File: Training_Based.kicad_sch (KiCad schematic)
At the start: 66 parts

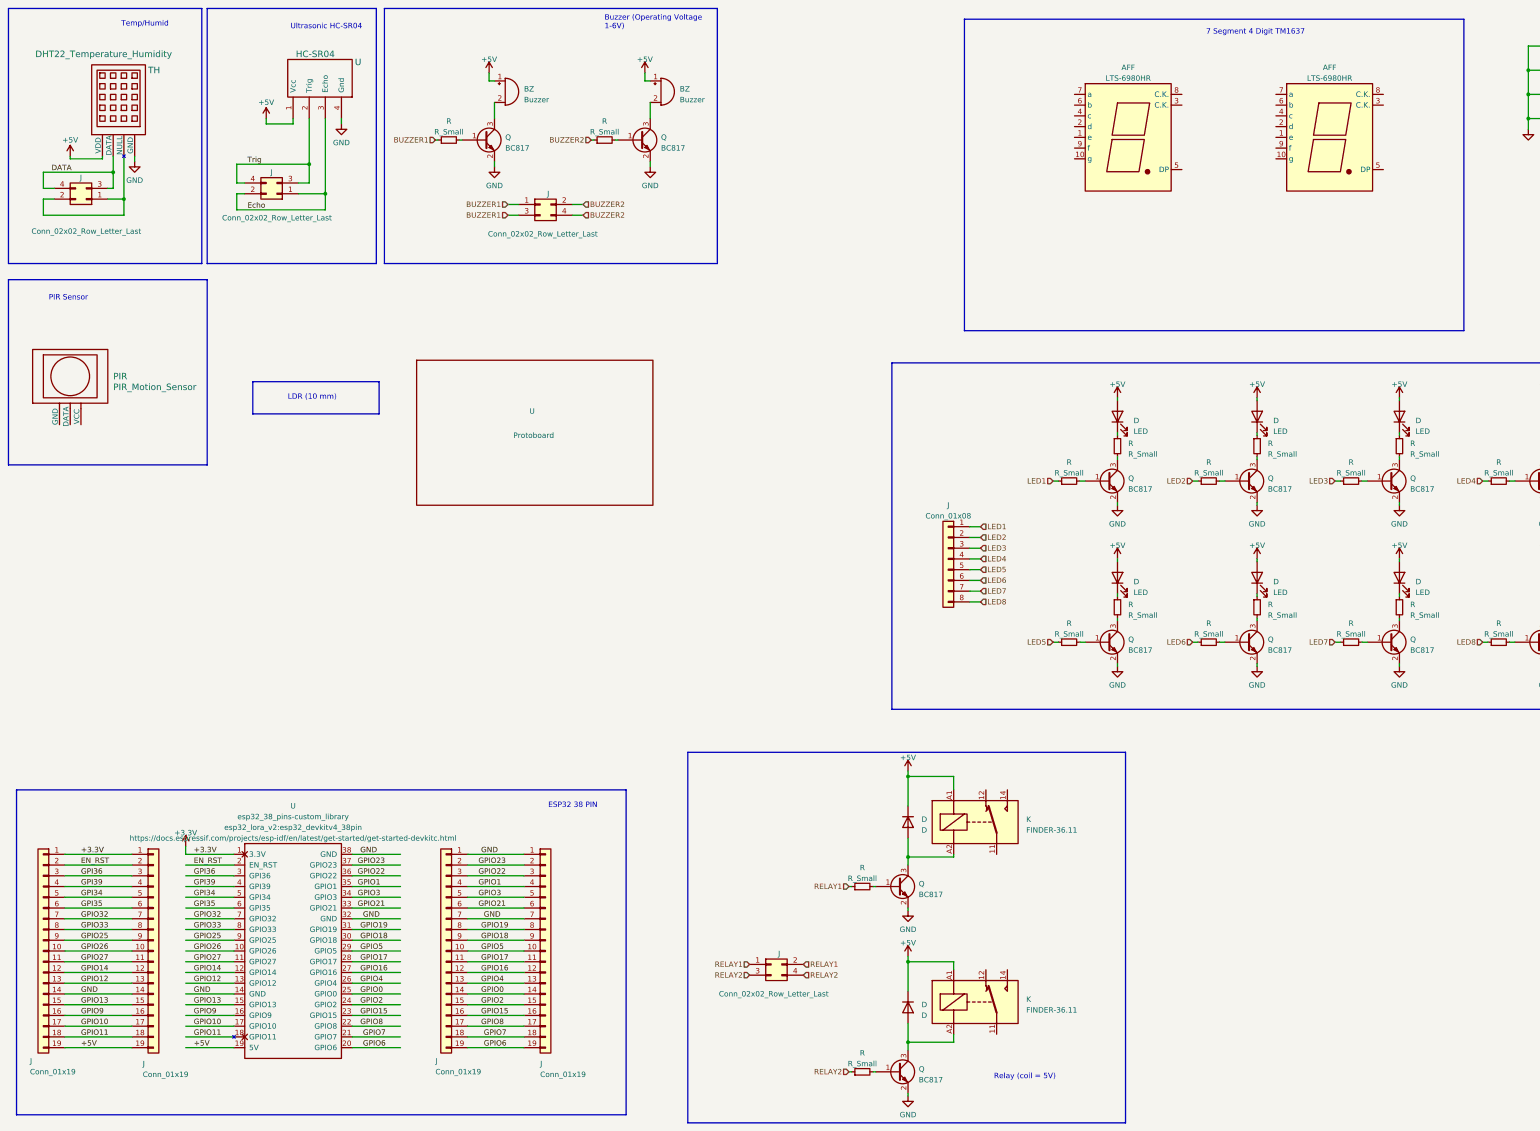
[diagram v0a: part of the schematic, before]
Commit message: 7 segment and relay
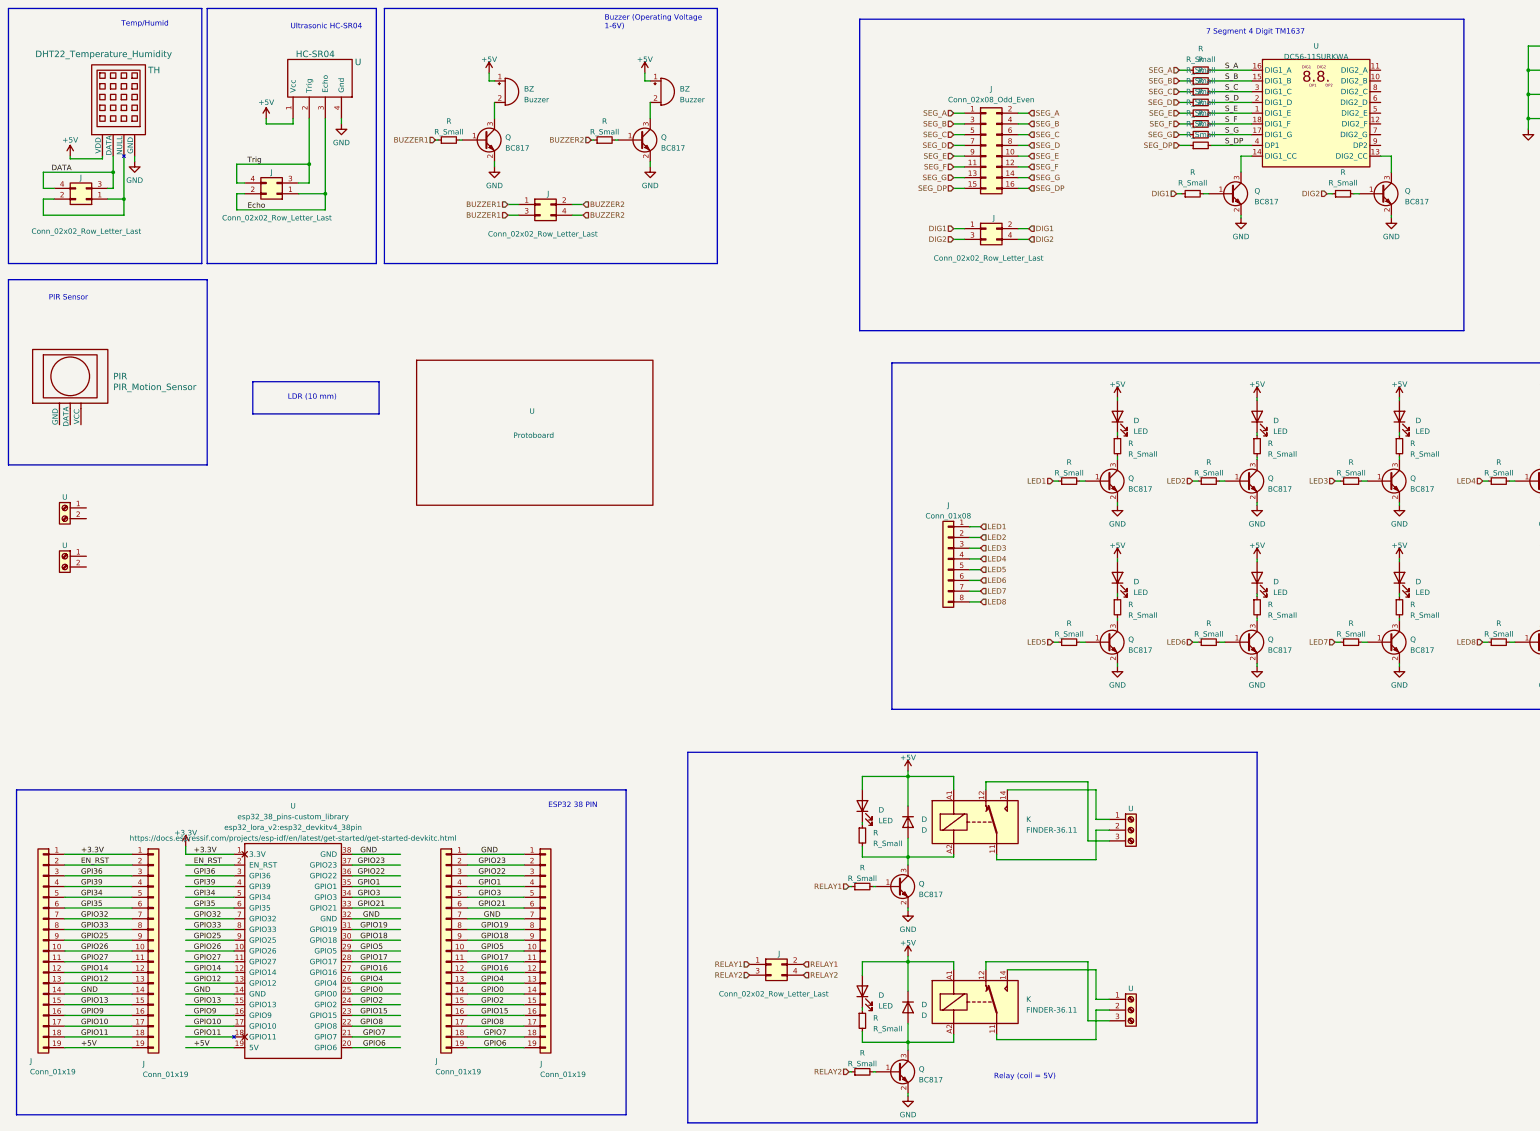
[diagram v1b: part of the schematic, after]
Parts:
- removed AFF (x2): LTS-6980HR, Display_7Segment:7SegmentLED_LTS6760_LTS6780, symbol Display_Character:LTS-6980HR
- added D (x2): LED, symbol Device:LED
- added J: Conn_02x02_Row_Letter_Last, symbol Connector_Generic:Conn_02x02_Odd_Even
- added J: Conn_02x08_Odd_Even, symbol Connector_Generic:Conn_02x08_Odd_Even
- added Q (x2): BC817, Package_TO_SOT_SMD:SOT-23, symbol Transistor_BJT:BC817
- added R (x12): R_Small, symbol Device:R_Small
- added U: DC56-11SURKWA, Display_7Segment:DA56-11SURKWA, symbol Display_Character:DC56-11SURKWA
- added U (x2): (no value), symbol Connector:Screw_Terminal_01x03
- added U (x2): (no value), symbol Connector:Screw_Terminal_01x02
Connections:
- net +5V: now also D.2 (A), D.2 (A)
- net GND: now also Q.2 (E), Q.2 (E)
- net at K.11: now also U.2 (Pin_2) (x2)
- net at K.12: now also U.3 (Pin_3) (x2)
- net at K.14: now also U.1 (Pin_1) (x2)
- net at D.2 (A), K.A2, Q.3 (C): now also R.2 (x2)
- new net: D.1 (K), R.1 (x2)
- new net: Q.3 (C), U.13 (DIG2_CC)
- new net: Q.3 (C), U.14 (DIG1_CC)
- new net: Q.1 (B), R.2 (x2)
- new net DIG1: J.1 (Pin_1), J.2 (Pin_2), R.1
- new net DIG2: J.3 (Pin_3), J.4 (Pin_4), R.1
- new net SEG_A: J.1 (Pin_1), J.2 (Pin_2), R.1
- new net SEG_B: J.3 (Pin_3), J.4 (Pin_4), R.1
- new net SEG_C: J.5 (Pin_5), J.6 (Pin_6), R.1
- new net SEG_D: J.7 (Pin_7), J.8 (Pin_8), R.1
- new net SEG_DP: J.15 (Pin_15), J.16 (Pin_16), R.1
- new net SEG_E: J.10 (Pin_10), J.9 (Pin_9), R.1
- new net SEG_F: J.11 (Pin_11), J.12 (Pin_12), R.1
- new net SEG_G: J.13 (Pin_13), J.14 (Pin_14), R.1
- new net S_A: R.2, U.16 (DIG1_A)
- new net S_B: R.2, U.15 (DIG1_B)
- new net S_C: R.2, U.3 (DIG1_C)
- new net S_D: R.2, U.2 (DIG1_D)
- new net S_DP: R.2, U.4 (DP1)
- new net S_E: R.2, U.1 (DIG1_E)
- new net S_F: R.2, U.18 (DIG1_F)
- new net S_G: R.2, U.17 (DIG1_G)

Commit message: opto isolator
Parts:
- added J (x2): Conn_01x03, symbol Connector_Generic:Conn_01x03
- added J (x2): Conn_02x02_Row_Letter_Last, symbol Connector_Generic:Conn_02x02_Odd_Even
- added R (x4): R_Small, symbol Device:R_Small
- added U (x2): LTV-827, Package_DIP:DIP-8_W7.62mm, symbol Isolator:LTV-827
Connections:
- net +3.3V: now also R.2, R.2
- net +5V: now also J.2 (Pin_2), J.2 (Pin_2)
- net GND: now also J.3 (Pin_3), J.3 (Pin_3), U.7, U.7
- net at U.1 (Pin_1): now also R.1 (x2)
- net at U.2 (Pin_2): now also U.2 (x2)
- new net: R.2, U.1 (x2)
- new net POTO_OUT1: J.1 (Pin_1), J.2 (Pin_2), R.1, U.8
- new net POTO_OUT2: J.3 (Pin_3), J.4 (Pin_4), R.1, U.8
- new net SERVO1: J.1 (Pin_1), J.1 (Pin_1), J.2 (Pin_2)
- new net SERVO2: J.1 (Pin_1), J.3 (Pin_3), J.4 (Pin_4)
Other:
- note added: "Servo Motor"
- moved on the sheet: U

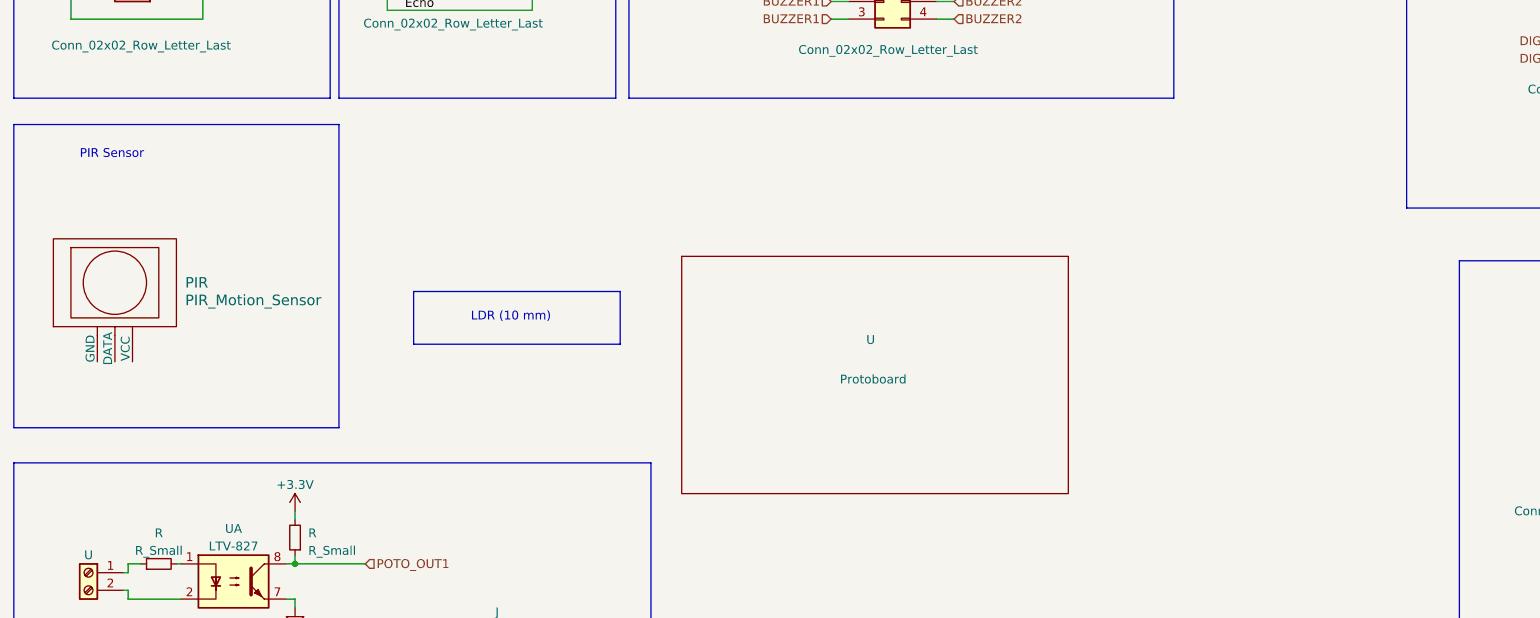
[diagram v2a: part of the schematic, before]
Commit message: update Optoelectronic parts
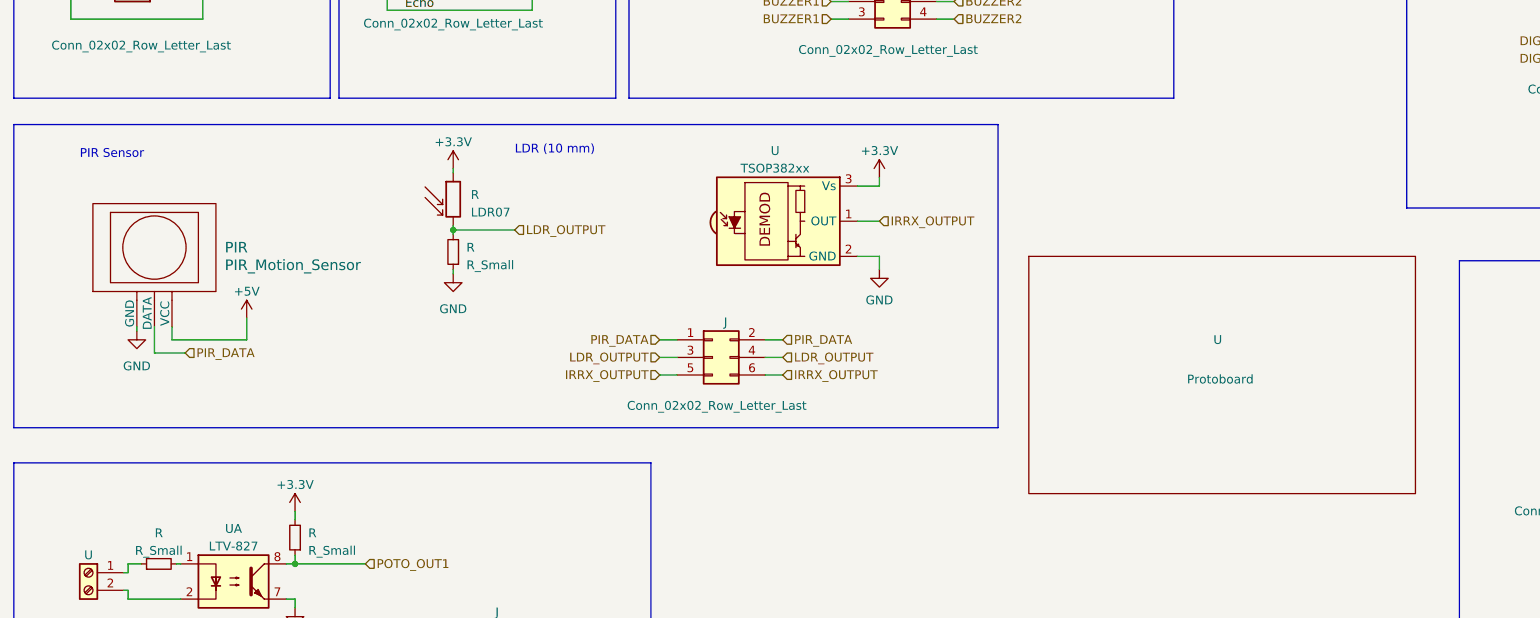
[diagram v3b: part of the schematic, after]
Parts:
- added J: Conn_02x02_Row_Letter_Last, symbol Connector_Generic:Conn_02x03_Odd_Even
- added R: LDR07, OptoDevice:R_LDR_5.1x4.3mm_P3.4mm_Vertical, symbol Sensor_Optical:LDR07
- added R: R_Small, symbol Device:R_Small
- added U: TSOP382xx, OptoDevice:Vishay_MINICAST-3Pin, symbol Interface_Optical:TSOP382xx
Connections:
- net +3.3V: now also R.1, U.3 (Vs)
- net +5V: now also PIR.3 (VCC)
- net GND: now also PIR.1 (GND), R.1, U.2 (GND)
- net PIR_DATA: now reaches PIR.2 (DATA)
- net PIR_DATA: now also J.1 (Pin_1), J.2 (Pin_2)
- new net IRRX_OUTPUT: J.5 (Pin_5), J.6 (Pin_6), U.1 (OUT)
- new net LDR_OUTPUT: J.3 (Pin_3), J.4 (Pin_4), R.2, R.2
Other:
- moved on the sheet: PIR, U

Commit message: add tact switch and rotary switch
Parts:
- added D (x2): LED, symbol Device:LED
- added J: Conn_02x07_Odd_Even, symbol Connector_Generic:Conn_02x05_Odd_Even
- added R (x4): R_Small, symbol Device:R_Small
- added SW: RotaryEncoder_Switch, symbol Device:RotaryEncoder_Switch
- added SW (x2): SW_Push, symbol Switch:SW_Push
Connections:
- net +3.3V: now also R.1, R.1
- net +5V: now also D.2 (A), D.2 (A)
- net GND: now also SW.1, SW.1, SW.C, SW.S2
- net S_A: now also U.11 (DIG2_A)
- net S_B: now also U.10 (DIG2_B)
- net S_C: now also U.8 (DIG2_C)
- net S_D: now also U.6 (DIG2_D)
- net S_DP: now also U.9 (DP2)
- net S_E: now also U.5 (DIG2_E)
- net S_F: now also U.12 (DIG2_F)
- net S_G: now also U.7 (DIG2_G)
- new net: D.1 (K), R.1 (x2)
- new net A_Rotary: J.3 (Pin_3), J.4 (Pin_4), SW.A
- new net B_Rotary: J.5 (Pin_5), J.6 (Pin_6), SW.B
- new net S1_PB: J.7 (Pin_7), J.8 (Pin_8), R.2, R.2, SW.2
- new net S1_Rotary: J.1 (Pin_1), J.2 (Pin_2), SW.S1
- new net S2_PB: J.10 (Pin_10), J.9 (Pin_9), R.2, R.2, SW.2
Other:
- moved on the sheet: D, J, K, PIR, Q, R, U, UA

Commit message: finish layout
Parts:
- added C (x2): C_Polarized_US, symbol Device:C_Polarized_Small_US
- added J: Conn_02x02_Row_Letter_Last, symbol Connector_Generic:Conn_02x02_Odd_Even
- added J: USB_B_Mini, symbol Connector:USB_B_Mini
- added J (x2): Conn_01x08, symbol Connector_Generic:Conn_01x08
- added J (x3): Conn_02x07_Odd_Even, symbol Connector_Generic:Conn_02x05_Odd_Even
- added R (x2): R_Small, symbol Device:R_Small
- added RV: R_Potentiometer, symbol Device:R_Potentiometer
- added U (x2): (no value), symbol ESP32-PoE-ISO_Rev_D:R
- added U (x3): (no value), symbol ESP32-PoE-ISO_Rev_D:C
- added U: (no value), symbol Device:Polyfuse
- added U: (no value), symbol Custom_Library:SY8009AAAC(SOT23-5)
- added U: (no value), symbol ESP32-PoE-ISO_Rev_D:L
- added U: (no value), symbol Connector:Screw_Terminal_01x02
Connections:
- net +3.3V: now also C.1, J.1 (Pin_1), J.10 (Pin_10), J.2 (Pin_2), J.3 (Pin_3), J.4 (Pin_4), J.5 (Pin_5), J.6 (Pin_6), J.7 (Pin_7), J.8 (Pin_8), J.9 (Pin_9), RV.1, U.1, U.1, U.1, U.2
- net +5V: now also C.1, J.1 (Pin_1), J.10 (Pin_10), J.2 (Pin_2), J.3 (Pin_3), J.4 (Pin_4), J.5 (Pin_5), J.6 (Pin_6), J.7 (Pin_7), J.8 (Pin_8), J.9 (Pin_9)
- net GND: now also C.2, C.2, J.1 (Pin_1), J.10 (Pin_10), J.2 (Pin_2), J.3 (Pin_3), J.4 (Pin_4), J.5 (GND), J.5 (Pin_5), J.6 (Pin_6), J.6 (Shield), J.7 (Pin_7), J.8 (Pin_8), J.9 (Pin_9), R.1, RV.3, U.2, U.2, U.2, U.2 (GND), U.2 (Pin_2)
- new net: U.1, U.2, U.2, U.5 (FB)
- new net: J.1 (VBUS), U.2
- new net: R.2, U.1 (Pin_1)
- new net Analog_Input: J.3 (Pin_3), J.4 (Pin_4), R.1, R.2
- new net IN: U.1, U.1, U.1 (EN), U.4 (IN)
- new net LX: U.1, U.3 (LX)
- new net Poten_voltage: J.1 (Pin_1), J.2 (Pin_2), RV.2
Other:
- moved on the sheet: U

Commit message: Update Training_Based.kicad_sch
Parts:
- added D: LED, symbol Device:LED
- added R: R_Small, symbol Device:R_Small
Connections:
- net IN is gone; now on net +5V: U.1, U.1, U.1 (EN), U.4 (IN)
- net +5V: now also D.2 (A)
- net GND: now also R.2
- new net: D.1 (K), R.1
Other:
- moved on the sheet: J, K, R
